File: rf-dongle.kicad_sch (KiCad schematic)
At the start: 40 parts, among them J1 USB_A, J3 TC2030, SW1 SW_Push, SW2 SW_Push, U1 nRF52840-QIXX, X1 32MHz, X2 32.768kHz

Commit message: rework programming pins, cleanup pcb routing
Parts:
- removed J3: TC2030, Connector:Tag-Connect_TC2030-IDC-NL_2x03_P1.27mm_Vertical, symbol Connector:TC2030
- removed SW2: SW_Push, Button_Switch_SMD:SW_SPST_B3U-1000P, symbol Switch:SW_Push
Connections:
- no-connect marks 46 -> 45
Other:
- note added: "Most of the schematic is a direct copy of the reference schematic for the QFAA layout. The only exceptions are the LEDs, programming pins and reset button."
- note added: "Optional shield left floating, since it's grounded by the host."
- note added: "Programming pins (SWD)"
- note added: "RF Dongle (based on nRF52840 QIAA)"
- note added: "Reset pin can technically be configured to either reset on connect or disconnect, but it's pulled up on nRF52-DK and Dongle, so pulling it up here as well."
- note added: "The antenna should have its own matching network, used to tune the antenna's frequency, omitting it for now, since I have no way to tune such the components after the PCB is produced."
- note added: "These are the pins from a TC2030 connector broken out and spread around the board because the connector was too big to fit in any one place"
- note removed: "Antenna matching network, used to reduce noise from the antenna's output."
- note removed: "Configurable Button"
- note removed: "JTAG Connector (SWD)"
- note removed: "Most of the schematic is a direct copy of the reference schematic for the QFAA layout. The only exceptions are the LEDs, configurable button, programming pins and reset button."
- note removed: "RF Dongle (based on nRF52840)"
- note removed: "Reset pin can technically be configured to either reset on connect or disconnect, but it's pulled up on nRF52-DK and Dongle, so leaving it pulled up here as well."
- note removed: "Shield left floating since it's grounded by the host."
- note removed: "TODO: - [ ] Select components - [ ] Inductor - [ ] Capacitors - [ ] Resistor - [ ] Antenna (?) - [ ] Define pins for LEDs - [ ] Define pins for Button"
- note removed: "The pinout for the connector is custom to simplify routing."
- note removed: "User configurable button (e.g. for pairing). GPIO pins have an internal 13k pull-up resistor, so one is not needed here. Also this is the same setup as the nRF52-DK"
- moved on the sheet: D2, D3, H1, H2, H3, H4, H5, R2, R3, R4, SW1

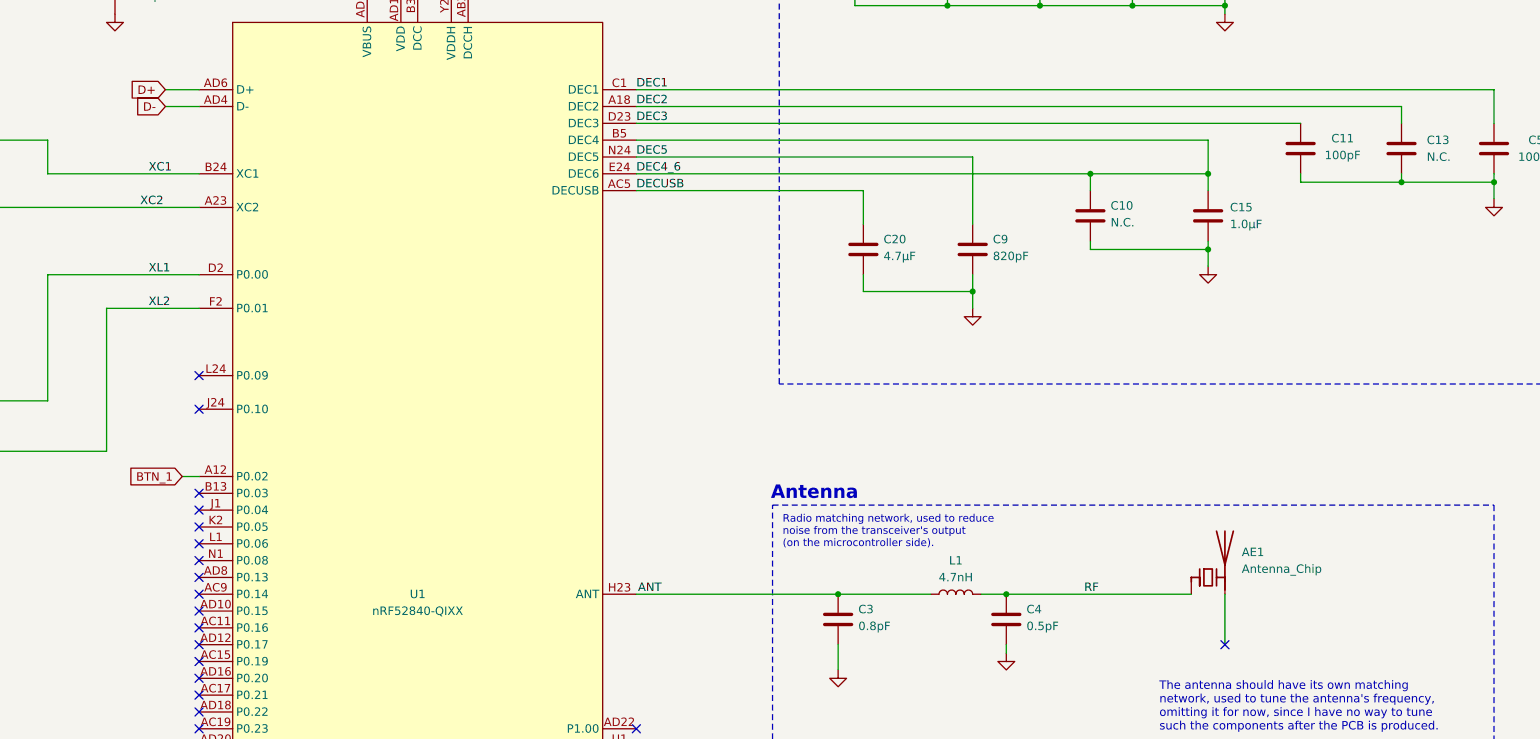
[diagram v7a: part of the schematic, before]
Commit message: adjust footprints for handsoldering, tweak antenna
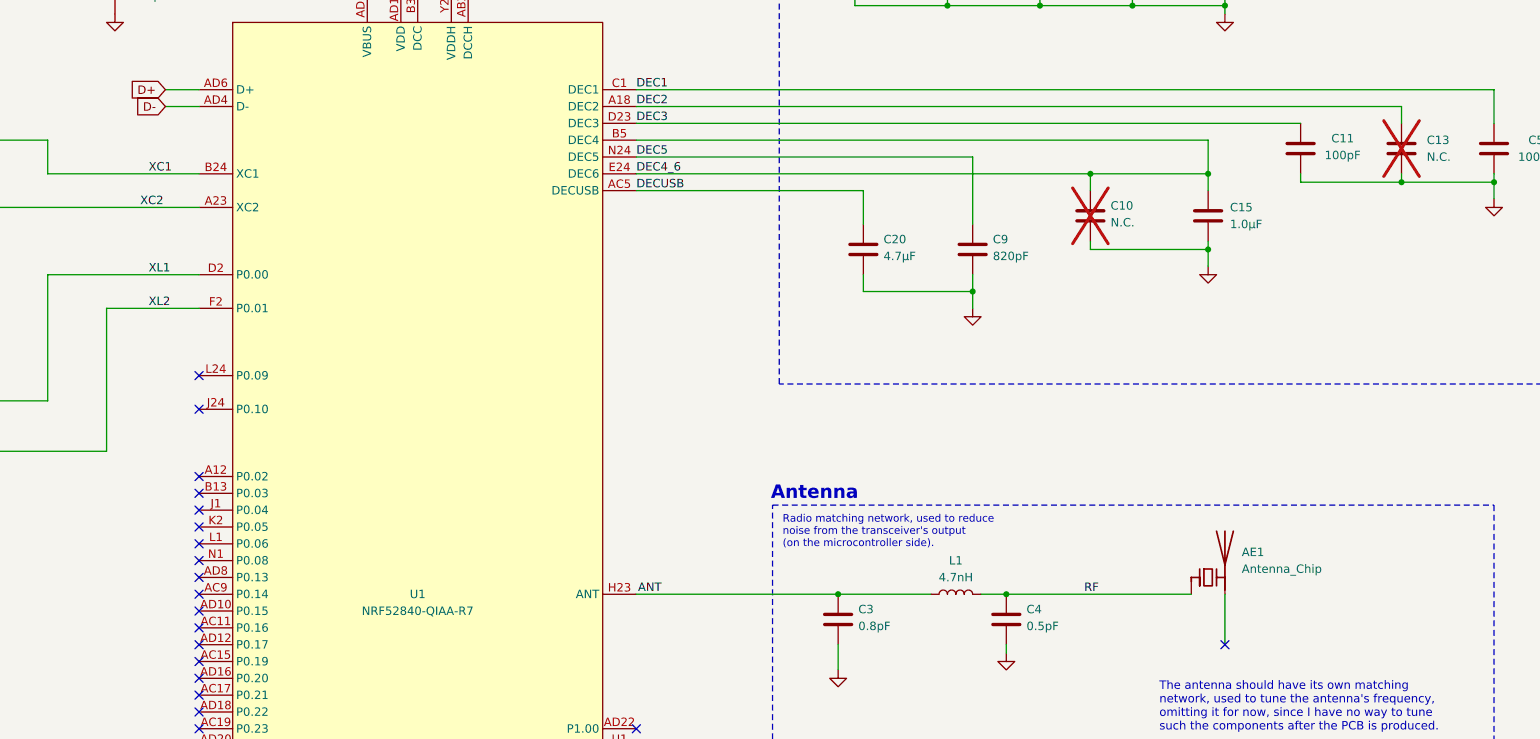
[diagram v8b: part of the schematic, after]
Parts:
- AE1: JLC PN (none) -> C89334
- C1, C11, C12, C17, C18, C2, C3, C4, C5, C7, C8, C9: footprint Capacitor_SMD:C_0402_1005Metric -> Capacitor_SMD:C_0402_1005Metric_Pad0.74x0.62mm_HandSolder
- C10, C13: footprint Capacitor_SMD:C_0402_1005Metric -> Capacitor_SMD:C_0402_1005Metric_Pad0.74x0.62mm_HandSolder; now not fitted
- C14, C15, C19, C20, C6: footprint Capacitor_SMD:C_0603_1608Metric -> Capacitor_SMD:C_0603_1608Metric_Pad1.08x0.95mm_HandSolder
- D1: JLC PN (none) -> C5337179
- D2: footprint LED_SMD:LED_0402_1005Metric -> LED_SMD:LED_0402_1005Metric_Pad0.77x0.64mm_HandSolder; JLC PN (none) -> C165980
- D3: footprint LED_SMD:LED_0402_1005Metric -> LED_SMD:LED_0402_1005Metric_Pad0.77x0.64mm_HandSolder; JLC PN (none) -> C165979
- L1: footprint Inductor_SMD:L_0402_1005Metric -> Inductor_SMD:L_0402_1005Metric_Pad0.77x0.64mm_HandSolder
- R1, R2: footprint Resistor_SMD:R_0402_1005Metric -> Resistor_SMD:R_0402_1005Metric_Pad0.72x0.64mm_HandSolder
- R3, R4: footprint Resistor_SMD:R_0201_0603Metric -> Resistor_SMD:R_0402_1005Metric_Pad0.72x0.64mm_HandSolder; JLC PN (none) -> C784160
- SW1: JLC PN (none) -> C231329
- U1: value nRF52840-QIXX -> NRF52840-QIAA-R7; JLC PN (none) -> C1851953
- X2: footprint Crystal:Crystal_SMD_2012-2Pin_2.0x1.2mm -> Crystal:Crystal_SMD_2012-2Pin_2.0x1.2mm_HandSoldering; JLC PN (none) -> C97603
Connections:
- net BTN_1: no longer names the net of U1.A12 (P0.02)
- no-connect marks 45 -> 46
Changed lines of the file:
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@@
 	)
 	(no_connect
+		(at 165.1 119.38)
+	)
+	(no_connect
 		(at 165.1 198.12)
 	)
@@
 	(wire
 		(pts
-			(xy 162.56 119.38) (xy 165.1 119.38)
-		)
-		(stroke
-			(width 0)
-			(type default)
-		)
-	)
-	(wire
-		(pts
 			(xy 306.07 46.99) (xy 306.07 48.26)
 		)
@@
 		)
 	)
-	(global_label "BTN_1"
-		(shape input)
-		(at 162.56 119.38 180)
-		(fields_autoplaced yes)
-		(effects
-			(font
-				(size 1.27 1.27)
-			)
-			(justify right)
-		)
-		(property "Intersheetrefs" "${INTERSHEET_REFS}"
-			(at 153.8296 119.38 0)
-			(effects
-				(font
-					(size 1.27 1.27)
-				)
-				(justify right)
-				(hide yes)
-			)
-		)
-	)
 	(global_label "RESET"
 		(shape input)
@@
 			)
 		)
+		(property "JLC PN" ""
+			(at 106.68 73.66 90)
+			(effects
+				(font
+					(size 1.27 1.27)
+				)
+				(hide yes)
+			)
+		)
 		(pin "1"
 		)
@@
 			)
 		)
-		(property "Footprint" "Capacitor_SMD:C_0402_1005Metric"
+		(property "Footprint" "Capacitor_SMD:C_0402_1005Metric_Pad0.74x0.62mm_HandSolder"
 			(at 305.1048 39.37 0)
 			(effects
@@
 			)
 		)
-		(property "Footprint" "Capacitor_SMD:C_0402_1005Metric"
+		(property "Footprint" "Capacitor_SMD:C_0402_1005Metric_Pad0.74x0.62mm_HandSolder"
 			(at 286.0548 137.16 0)
 			(effects
@@
 			)
 		)
-		(property "Footprint" "LED_SMD:LED_0402_1005Metric"
+		(property "Footprint" "LED_SMD:LED_0402_1005Metric_Pad0.77x0.64mm_HandSolder"
 			(at 238.76 252.73 0)
 			(effects
@@
 			)
 		)
+		(property "JLC PN" "C165980"
+			(at 238.76 252.73 0)
+			(effects
+				(font
+					(size 1.27 1.27)
+				)
+				(hide yes)
+			)
+		)
 		(pin "2"
 		)
@@
 			)
 		)
-		(property "Footprint" "Capacitor_SMD:C_0402_1005Metric"
+		(property "Footprint" "Capacitor_SMD:C_0402_1005Metric_Pad0.74x0.62mm_HandSolder"
 			(at 86.36 79.7052 0)
 			(effects
@@
 			)
 		)
-		(property "Footprint" "Resistor_SMD:R_0402_1005Metric"
+		(property "Footprint" "Resistor_SMD:R_0402_1005Metric_Pad0.72x0.64mm_HandSolder"
 			(at 139.7 38.862 90)
 			(effects
@@
 			)
 		)
-		(property "Value" "nRF52840-QIXX"
+		(property "Value" "NRF52840-QIAA-R7"
 			(at 198.12 139.7 0)
 			(do_not_autoplace yes)
@@
 			)
 		)
+		(property "JLC PN" "C1851953"
+			(at 198.12 137.16 0)
+			(effects
+				(font
+					(size 1.27 1.27)
+				)
+				(hide yes)
+			)
+		)
 		(pin "H23"
 		)
@@
 		(in_bom yes)
 		(on_board yes)
-		(dnp no)
+		(dnp yes)
 		(property "Reference" "C13"
 			(at 350.52 68.5799 0)
@@
 			)
 		)
-		(property "Footprint" "Capacitor_SMD:C_0402_1005Metric"
+		(property "Footprint" "Capacitor_SMD:C_0402_1005Metric_Pad0.74x0.62mm_HandSolder"
 			(at 347.6752 73.66 0)
 			(effects
@@
 			)
 		)
+		(property "JLC PN" "C5337179"
+			(at 101.6 170.18 90)
+			(effects
+				(font
+					(size 1.27 1.27)
+				)
+				(hide yes)
+			)
+		)
 		(pin "3"
 		)
@@
 			)
 		)
-		(property "Footprint" "Capacitor_SMD:C_0402_1005Metric"
+		(property "Footprint" "Capacitor_SMD:C_0402_1005Metric_Pad0.74x0.62mm_HandSolder"
 			(at 280.9748 81.28 0)
 			(effects
@@
 			)
 		)
-		(property "Footprint" "Capacitor_SMD:C_0402_1005Metric"
+		(property "Footprint" "Capacitor_SMD:C_0402_1005Metric_Pad0.74x0.62mm_HandSolder"
 			(at 277.1648 39.37 0)
 			(effects
@@
 			)
 		)
-		(property "Footprint" "Capacitor_SMD:C_0603_1608Metric"
+		(property "Footprint" "Capacitor_SMD:C_0603_1608Metric_Pad1.08x0.95mm_HandSolder"
 			(at 263.1948 39.37 0)
 			(effects
@@
 			)
 		)
-		(property "Footprint" "Capacitor_SMD:C_0402_1005Metric"
+		(property "Footprint" "Capacitor_SMD:C_0402_1005Metric_Pad0.74x0.62mm_HandSolder"
 			(at 87.63 116.5352 0)
 			(effects
@@
 			)
 		)
-		(property "Footprint" "Capacitor_SMD:C_0402_1005Metric"
+		(property "Footprint" "Capacitor_SMD:C_0402_1005Metric_Pad0.74x0.62mm_HandSolder"
 			(at 291.1348 39.37 0)
 			(effects
@@
 			)
 		)
-		(property "Footprint" "Capacitor_SMD:C_0603_1608Metric"
+		(property "Footprint" "Capacitor_SMD:C_0603_1608Metric_Pad1.08x0.95mm_HandSolder"
 			(at 319.0748 39.37 0)
 			(effects
@@
 			)
 		)
-		(property "Footprint" "Capacitor_SMD:C_0603_1608Metric"
+		(property "Footprint" "Capacitor_SMD:C_0603_1608Metric_Pad1.08x0.95mm_HandSolder"
 			(at 151.4348 41.91 0)
 			(effects
@@
 			)
 		)
-		(property "Footprint" "Resistor_SMD:R_0402_1005Metric"
+		(property "Footprint" "Resistor_SMD:R_0402_1005Metric_Pad0.72x0.64mm_HandSolder"
 			(at 111.252 254 90)
 			(effects
@@
 			)
 		)
-		(property "Footprint" "Capacitor_SMD:C_0402_1005Metric"
+		(property "Footprint" "Capacitor_SMD:C_0402_1005Metric_Pad0.74x0.62mm_HandSolder"
 			(at 93.98 67.6148 0)
 			(effects
@@
 			)
 		)
-		(property "Footprint" "Capacitor_SMD:C_0402_1005Metric"
+		(property "Footprint" "Capacitor_SMD:C_0402_1005Metric_Pad0.74x0.62mm_HandSolder"
 			(at 95.25 106.9848 0)
 			(effects
@@
 			)
 		)
-		(property "Footprint" "Capacitor_SMD:C_0402_1005Metric"
+		(property "Footprint" "Capacitor_SMD:C_0402_1005Metric_Pad0.74x0.62mm_HandSolder"
 			(at 260.6548 137.16 0)
 			(effects
@@
 		(in_bom yes)
 		(on_board yes)
-		(dnp no)
+		(dnp yes)
 		(property "Reference" "C10"
 			(at 302.768 78.486 0)
@@
 			)
 		)
-		(property "Footprint" "Capacitor_SMD:C_0402_1005Metric"
+		(property "Footprint" "Capacitor_SMD:C_0402_1005Metric_Pad0.74x0.62mm_HandSolder"
 			(at 298.7548 76.2 0)
 			(effects
@@
 			)
 		)
+		(property "JLC PN" "C89334"
+			(at 317.5 134.62 0)
+			(effects
+				(font
+					(size 1.27 1.27)
+				)
+				(hide yes)
+			)
+		)
 		(pin "2"
 		)
@@
 			)
 		)
-		(property "Footprint" "Resistor_SMD:R_0201_0603Metric"
+		(property "Footprint" "Resistor_SMD:R_0402_1005Metric_Pad0.72x0.64mm_HandSolder"
 			(at 228.6 254.508 90)
 			(effects
@@
 			)
 		)
+		(property "JLC PN" "C784160"
+			(at 228.6 252.73 90)
+			(effects
+				(font
+					(size 1.27 1.27)
+				)
+				(hide yes)
+			)
+		)
 		(pin "1"
 		)
@@
 			)
 		)
-		(property "Footprint" "Capacitor_SMD:C_0603_1608Metric"
+		(property "Footprint" "Capacitor_SMD:C_0603_1608Metric_Pad1.08x0.95mm_HandSolder"
 			(at 264.4648 81.28 0)
 			(effects
@@
 			)
 		)
+		(property "JLC PN" "C231329"
+			(at 101.6 262.89 0)
+			(effects
+				(font
+					(size 1.27 1.27)
+				)
+				(hide yes)
+			)
+		)
 		(pin "2"
 		)
@@
 			)
 		)
-		(property "Footprint" "LED_SMD:LED_0402_1005Metric"
+		(property "Footprint" "LED_SMD:LED_0402_1005Metric_Pad0.77x0.64mm_HandSolder"
 			(at 238.76 265.43 0)
 			(effects
@@
 			)
 		)
+		(property "JLC PN" "C165979"
+			(at 238.76 265.43 0)
+			(effects
+				(font
+					(size 1.27 1.27)
+				)
+				(hide yes)
+			)
+		)
 		(pin "2"
 		)
@@
 			)
 		)
-		(property "Footprint" "Inductor_SMD:L_0402_1005Metric"
+		(property "Footprint" "Inductor_SMD:L_0402_1005Metric_Pad0.77x0.64mm_HandSolder"
 			(at 279.4 137.16 0)
 			(effects
@@
 			)
 		)
-		(property "Footprint" "Crystal:Crystal_SMD_2012-2Pin_2.0x1.2mm"
+		(property "Footprint" "Crystal:Crystal_SMD_2012-2Pin_2.0x1.2mm_HandSoldering"
 			(at 107.95 111.76 0)
 			(effects
@@
 			)
 		)
+		(property "JLC PN" "C97603"
+			(at 107.95 111.76 90)
+			(effects
+				(font
+					(size 1.27 1.27)
+				)
+				(hide yes)
+			)
+		)
 		(pin "2"
 		)
@@
 			)
 		)
-		(property "Footprint" "Capacitor_SMD:C_0402_1005Metric"
+		(property "Footprint" "Capacitor_SMD:C_0402_1005Metric_Pad0.74x0.62mm_HandSolder"
 			(at 332.4352 73.66 0)
 			(effects
@@
 			)
 		)
-		(property "Footprint" "Capacitor_SMD:C_0402_1005Metric"
+		(property "Footprint" "Capacitor_SMD:C_0402_1005Metric_Pad0.74x0.62mm_HandSolder"
 			(at 361.6452 73.66 0)
 			(effects
@@
 			)
 		)
-		(property "Footprint" "Resistor_SMD:R_0201_0603Metric"
+		(property "Footprint" "Resistor_SMD:R_0402_1005Metric_Pad0.72x0.64mm_HandSolder"
 			(at 228.6 267.208 90)
 			(effects
@@
 			)
 		)
+		(property "JLC PN" "C784160"
+			(at 228.6 265.43 90)
+			(effects
+				(font
+					(size 1.27 1.27)
+				)
+				(hide yes)
+			)
+		)
 		(pin "1"
 		)
@@
 			)
 		)
-		(property "Footprint" "Capacitor_SMD:C_0603_1608Metric"
+		(property "Footprint" "Capacitor_SMD:C_0603_1608Metric_Pad1.08x0.95mm_HandSolder"
 			(at 316.5348 76.2 0)
 			(effects
